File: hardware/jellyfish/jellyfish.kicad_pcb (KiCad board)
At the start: 4 copper layers, 80 x 70 mm, 164 parts, among them J1 INS, J10 Stemma QT, J2 8P8C_LED_Shielded, J3 CAM, J4 CAMLED, J5 OUT1, J6 BLTOUCH, J7 MOTOR, J8 MOTOR, J9 MOTOR, SW1 BOOTSEL, U1 VX7805-500, U10 TMC2209, U2 MIC5317-3.3, U3 RP2040, U4 W25Q128JVS, U5 74HC2G34, U6 TVS, U7 74HC2G34, U8 TMC2209, U9 TMC2209, Y1 12MHz

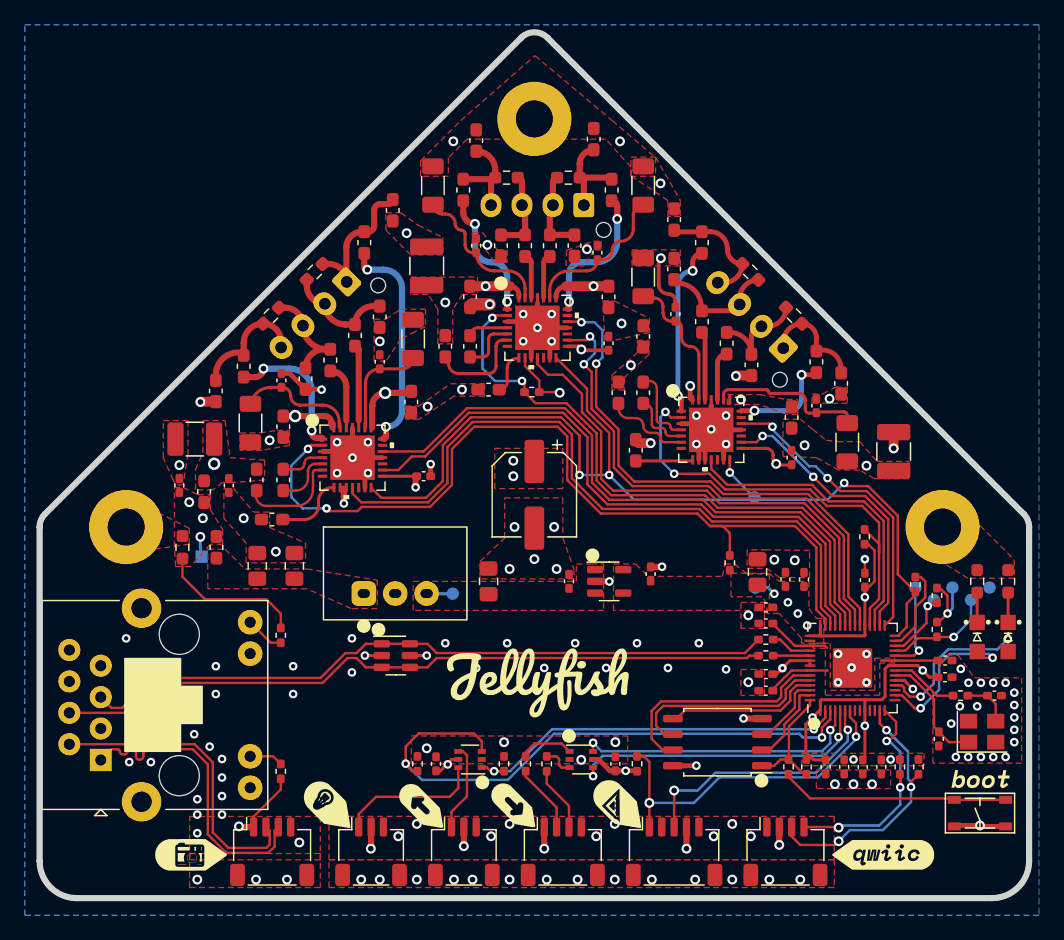
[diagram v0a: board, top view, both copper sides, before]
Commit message: Update Jellyfish with some stuff from Starfish
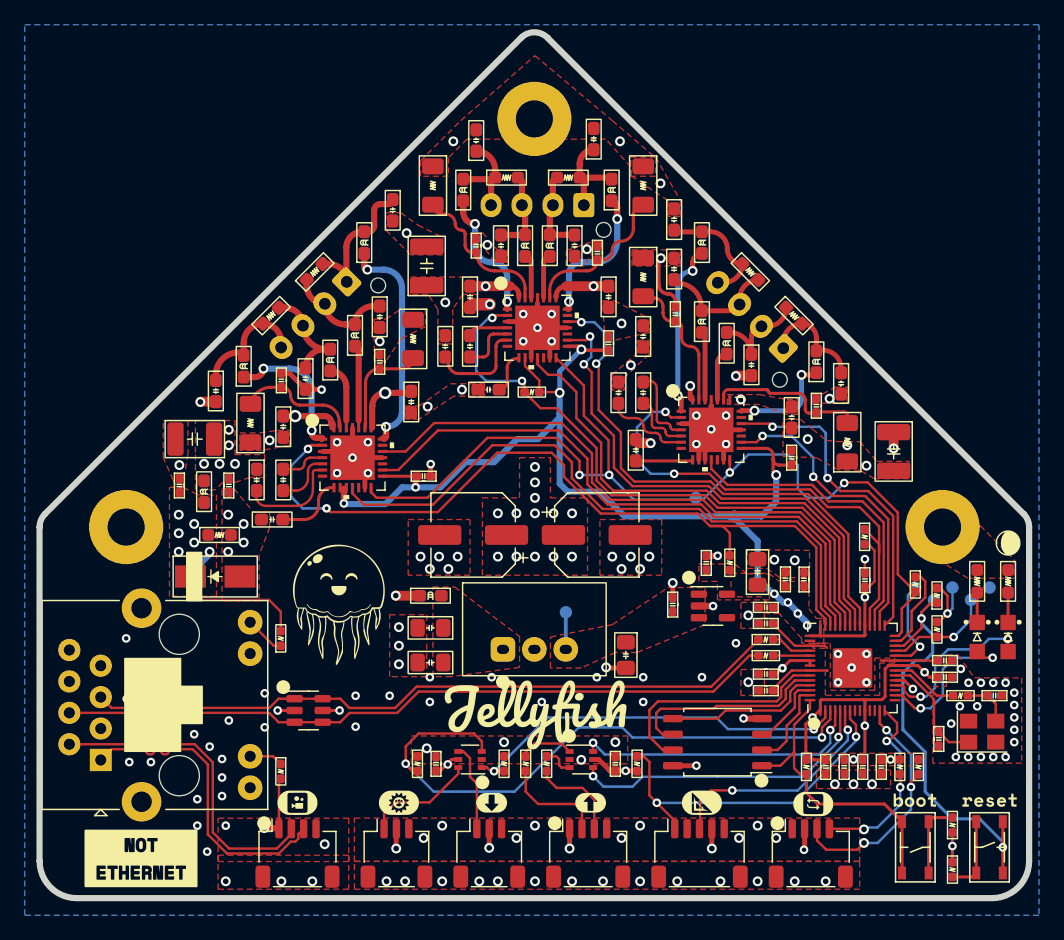
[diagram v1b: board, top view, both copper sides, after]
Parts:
- removed the ? at (105.4, 60.3)
- removed the ? at (113.4, 63.2)
- removed the ? at (105.3, 85.4)
- removed the ? at (133.6, 107.1)
- removed the ? at (111.9, 103.0)
- removed the ? at (103.5, 103.1)
- removed the ? at (141.2, 101.0)
- removed the ? at (77.2, 107.1)
- removed the ? at (88.5, 103.1)
- removed the ? at (96.0, 103.2)
- removed the ? at (96.8, 63.2)
- added ?: , Graphics, F.Cu at (86.0, 102.9)
- added ?: , Graphics, F.Cu at (118.8, 102.9)
- added ?: , Graphics, F.Cu at (136.0, 102.7)
- added ?: , Graphics, F.Cu at (101.8, 102.9)
- added ?: , Graphics, B.Cu at (105.2, 91.7)
- added ?: , Graphics, B.Cu at (91.7, 67.9)
- added ?: , Graphics, B.Cu at (105.5, 60.8)
- added ?: , Graphics, B.Cu at (118.3, 68.0)
- added ?: , Graphics, F.Cu at (143.5, 81.9)
- added ?: , Graphics, F.Cu at (73.4, 107.4)
- added ?: , Graphics, F.Cu at (109.8, 102.9)
- added ?: , Graphics, F.Cu at (89.4, 86.9)
- added ?: , Graphics, F.Cu at (127.8, 103.0)
- added ?: , Graphics, F.Cu at (142.1, 102.7)
- added ?: , Graphics, F.Cu at (94.2, 102.9)
- added C22: 100u, Capacitor_SMD:CP_Elec_6.3x7.7, F.Cu at (100.2, 81.2)
- added D2: SMAJ28A, winterbloom:D_SMA, F.Cu at (79.4, 84.6)
- added R29: 1k, winterbloom:R_0402_HandSolder, F.Cu at (139.0, 108.3)
- added SW2: RESET, winterbloom:Tactile_Switch_4.2mm, F.Cu at (142.0, 106.5)
- C1, C11, C12, C13, C14, C15, C16, C17, C18, C19, C20, C21, C23, C24, C25, C26, C27, C29, C32, C33, C43, C46, C47, C57, C6, C60, C61, C7, C8, C9: footprint Capacitor_SMD:C_0402_1005Metric_Pad0.74x0.62mm_HandSolder -> winterbloom:C_0402_HandSolder
- C10, C2, C3, C4: footprint Capacitor_SMD:C_0805_2012Metric_Pad1.18x1.45mm_HandSolder -> winterbloom:C_0805_HandSolder
- C28, C30, C31, C36, C37, C38, C39, C40, C41, C42, C44, C45, C50, C51, C52, C53, C54, C55, C56, C58, C59, C64, C65, C66, C67, C68, C69: footprint Capacitor_SMD:C_0603_1608Metric_Pad1.08x0.95mm_HandSolder -> winterbloom:C_0603_HandSolder
- C35, C49, C63: footprint Capacitor_SMD:C_1210_3225Metric_Pad1.33x2.70mm_HandSolder -> winterbloom:C_1210_HandSolder
- FB1, FB10, FB11, FB12, FB13, FB14, FB2, FB3, FB4, FB5, FB6, FB7, FB8, FB9: footprint Inductor_SMD:L_0603_1608Metric_Pad1.05x0.95mm_HandSolder -> winterbloom:L_0603_HandSolder
- J1, J10, J3: footprint Connector_JST:JST_SH_SM04B-SRSS-TB_1x04-1MP_P1.00mm_Horizontal -> winterbloom:JST_SH_SM04B-SRSS-TB_1x04-1MP_P1.00mm_Horizontal
- J7, J8, J9: footprint Connector_JST:JST_XH_B4B-XH-AM_1x04_P2.50mm_Vertical -> winterbloom:JST_XH_B4B-XH-AM_1x04_P2.50mm_Vertical
- R1, R11, R12, R13, R14, R15, R16, R17, R2, R20, R23, R26, R27, R3, R4, R5, R6, R7, R8, R9: footprint Resistor_SMD:R_0402_1005Metric_Pad0.72x0.64mm_HandSolder -> winterbloom:R_0402_HandSolder
- R10, R28, RV1, RV2, RV3, RV4, RV5, RV6, RV7: footprint Resistor_SMD:R_0603_1608Metric_Pad0.98x0.95mm_HandSolder -> winterbloom:R_0603_HandSolder
- R18, R19, R21, R22, R24, R25: footprint Resistor_SMD:R_1206_3216Metric_Pad1.30x1.75mm_HandSolder -> winterbloom:R_1206_HandSolder
- moved ? 32.6 mm to (137.1, 102.2)
- moved FB14 17.7 mm to (96.8, 86.2), turned to 0 degrees
- moved C3 14.9 mm to (96.8, 88.8), turned to 180 degrees
- moved R9 14.1 mm to (139.0, 104.7)
- moved C2 13.5 mm to (96.8, 91.6), turned to 180 degrees
- moved C4 12.6 mm to (112.6, 91.0), turned to -90 degrees
- moved U1 12.1 mm to (102.7, 90.5)
- moved TP3 9.27 mm to (107.8, 87.5)
- moved U2 8.62 mm to (119.6, 87.0)
- moved C6 8.60 mm to (116.4, 86.9)
- moved U6 8.33 mm to (87.0, 95.4)
- moved C5 6.01 mm to (110.2, 81.2), turned to 0 degrees
- moved TP4 6.00 mm to (121.3, 79.8)
- moved SW1 5.91 mm to (136.0, 106.5), turned to 90 degrees
- moved TP17 4.75 mm to (118.2, 78.2)
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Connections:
- C30 pad 1: VMOTOR -> +24V
- C35 pad 1: VMOTOR -> +24V
- C36 pad 1: VMOTOR -> +24V
- C37 pad 1: VMOTOR -> +24V
- C44 pad 1: VMOTOR -> +24V
- C49 pad 1: VMOTOR -> +24V
- C5 pad 1: VMOTOR -> +24V
- C50 pad 1: VMOTOR -> +24V
- C51 pad 1: VMOTOR -> +24V
- C58 pad 1: VMOTOR -> +24V
- C63 pad 1: VMOTOR -> +24V
- C64 pad 1: VMOTOR -> +24V
- C65 pad 1: VMOTOR -> +24V
- C8 pad 1: +24V -> VDC
- C9 pad 1: VMOTOR -> +24V
- FB1 pad 1: +24V -> VDC
- FB1 pad 2: VMOTOR -> +24V
- FB14 pad 1: +24V -> VDC
- J2 pad 4: /Microcontroller/USB_D+ -> /Connections/MCU_D+
- J2 pad 5: /Microcontroller/USB_D- -> /Connections/MCU_D-
- J2 pad 6: +24V -> VDC
- J2 pad 8: +24V -> VDC
- R2 pad 2: +24V -> VDC
- R6 pad 1: /Microcontroller/USB_D+ -> /Connections/MCU_D+
- R6 pad 2: Net-(R6-Pad2) -> /Microcontroller/USB_D+
- R7 pad 1: /Microcontroller/USB_D- -> /Connections/MCU_D-
- R7 pad 2: Net-(R7-Pad2) -> /Microcontroller/USB_D-
- R9 pad 1: Net-(R9-Pad1) -> GND
- R9 pad 2: /Microcontroller/QSPI_CS -> Net-(R9-Pad2)
- RV1 pad 1: +24V -> VDC
- SW1 pad 1: Net-(R9-Pad1) -> /Microcontroller/QSPI_CS
- SW1 pad 2: GND -> Net-(R9-Pad2)
- TP2 pad 1: +24V -> VDC
- U10 pad 22: VMOTOR -> +24V
- U10 pad 28: VMOTOR -> +24V
- U3 pad 46: Net-(R7-Pad2) -> /Microcontroller/USB_D-
- U3 pad 47: Net-(R6-Pad2) -> /Microcontroller/USB_D+
- U6 pad 1: /Microcontroller/USB_D- -> /Connections/MCU_D-
- U6 pad 3: /Microcontroller/USB_D+ -> /Connections/MCU_D+
- U6 pad 4: /Microcontroller/USB_D+ -> /Connections/MCU_D+
- U6 pad 6: /Microcontroller/USB_D- -> /Connections/MCU_D-
- U8 pad 22: VMOTOR -> +24V
- U8 pad 28: VMOTOR -> +24V
- U9 pad 22: VMOTOR -> +24V
- U9 pad 28: VMOTOR -> +24V
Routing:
- net /Connections/MCU_D+: track 0.00 -> 58.1 mm
- net /Connections/MCU_D-: track 0.00 -> 56.3 mm
- net /Microcontroller/USB_D+: track 58.2 -> 2.97 mm
- net /Microcontroller/USB_D-: track 56.4 -> 3.35 mm
- net VDC: track 0.00 -> 33.3 mm, vias 0 -> 7
- net /Microcontroller/RUN: track 6.29 -> 36.6 mm, vias 1 -> 2
- net +5V: track 80.5 -> 102.7 mm
- net VMOTOR: track 22.0 -> 0.00 mm, vias 12 -> 0
- net Net-(R9-Pad1): track 17.7 -> 0.00 mm
- net /Microcontroller/QSPI_CS: track 9.52 -> 24.6 mm
- net +24V: track 13.3 -> 22.0 mm, vias 3 -> 27
- net Net-(R9-Pad2): track 0.00 -> 6.21 mm
- net Net-(R29-Pad2): track 0.00 -> 6.21 mm
- net /Microcontroller/M2_EN: track 69.6 -> 64.7 mm
- net /Microcontroller/M2_DIAG: track 56.0 -> 51.6 mm
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- added copper zone on F.Cu, net VDC
- added copper zone on In2.Cu, net VDC
- removed copper zone on F.Cu, net VMOTOR
- removed copper zone on In2.Cu, net VMOTOR
